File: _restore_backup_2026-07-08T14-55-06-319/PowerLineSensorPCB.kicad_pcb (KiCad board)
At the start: 4 copper layers, 115 x 47 mm, 248 parts, among them J1 SIM_Card_Shielded, J10 Conn_Coaxial, J11 Conn_Coaxial, J12 Conn_Coaxial, J13 Conn_Coaxial, J14 Conn_01x06_Pin, J15 Conn_01x03_MountingPin, J16 Conn_01x03_MountingPin, J17 Conn_01x03_MountingPin, J2 Micro_SD_Card, J3 Conn_Coaxial, J5 Conn_01x04_Pin, J6 USB_C_Receptacle_USB2.0_16P, J7 Conn_Coaxial, J8 Conn_01x04_Pin, SW1 SW_Push, SW2 SW_Push, SW3 SW_Push, U1 MLX90637, U10 BQ21080YBGR, U11 LM2903, U12 W25Q128JVE, U13 W25Q128JVE, U14 SKY65943-11, U2 ZTPD2210, U3 RP2350A, U4 RT6150BGQW, U5 TMAG5253BAx, U6 nRF9151-LAXX, U7 LIS2HH12, U8 RAK3172-xx-8-SM-xI, U9 P3T1755, Y1 Crystal_GND24

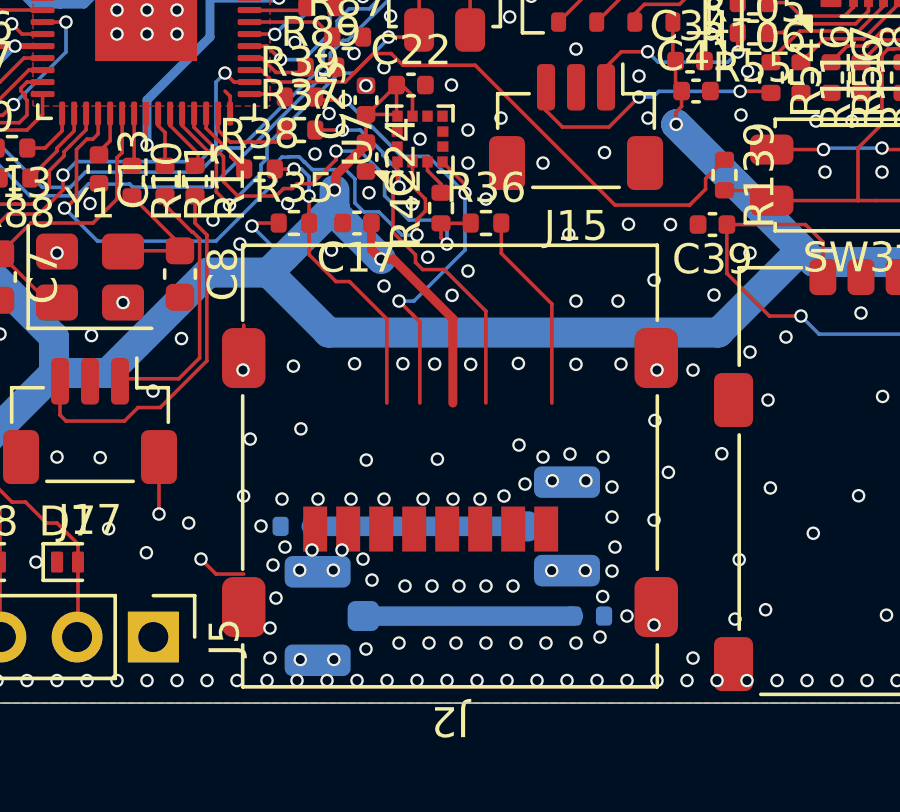
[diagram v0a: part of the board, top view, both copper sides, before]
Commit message: PCB development!!
Update submodule and add script for selecting non-GND vias

- Updated kicad-libs submodule to the latest commit.
- Added a new script `select_all_non_gnd_vias.py` to select all vias not connected to ground nets.
- Updated references in nRF9151 schematic from "IC1" to "U14" and from "AE1" to "ANT2".
- Modified temp_sensors schematic to add a hidden power input pin and adjusted component properties.
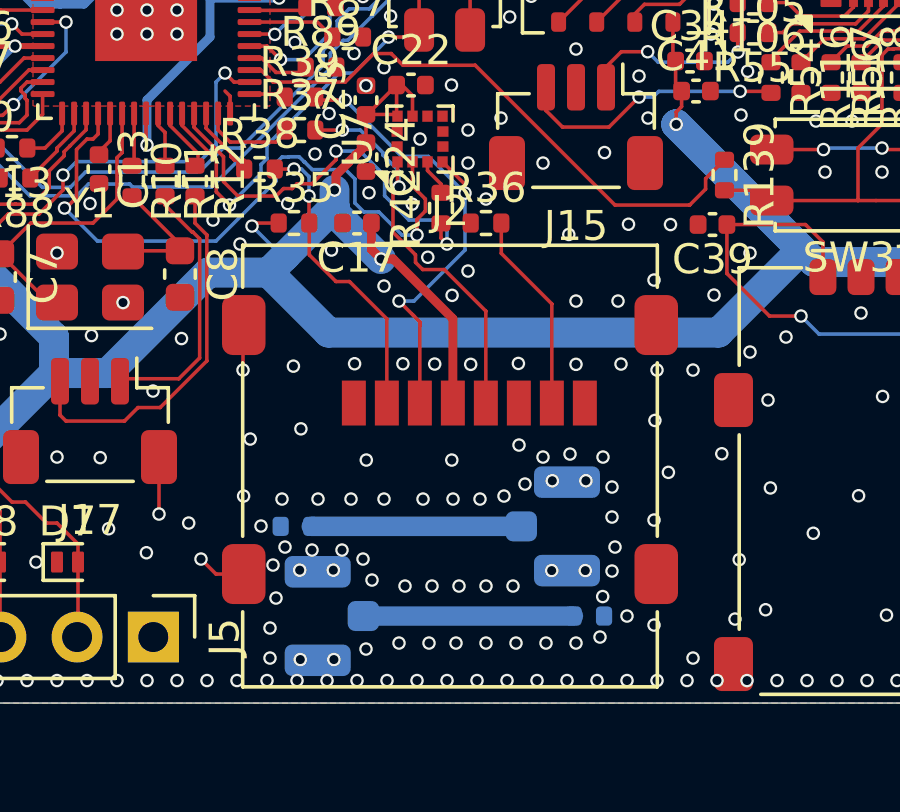
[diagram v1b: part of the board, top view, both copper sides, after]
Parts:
- U8: footprint BC_Processors:RAK3172 -> RF_Module:RAK3172
- turned J2 to 0 degrees
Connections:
- U1 pad 6: GND -> (no net)
